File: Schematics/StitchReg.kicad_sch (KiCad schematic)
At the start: 10 parts, among them J1 Barrel_Jack, J2 DIN-6, K1 DIPxx-1Axx-11x, SW1 SW_Push, U1 MCP4131-xxxx-P

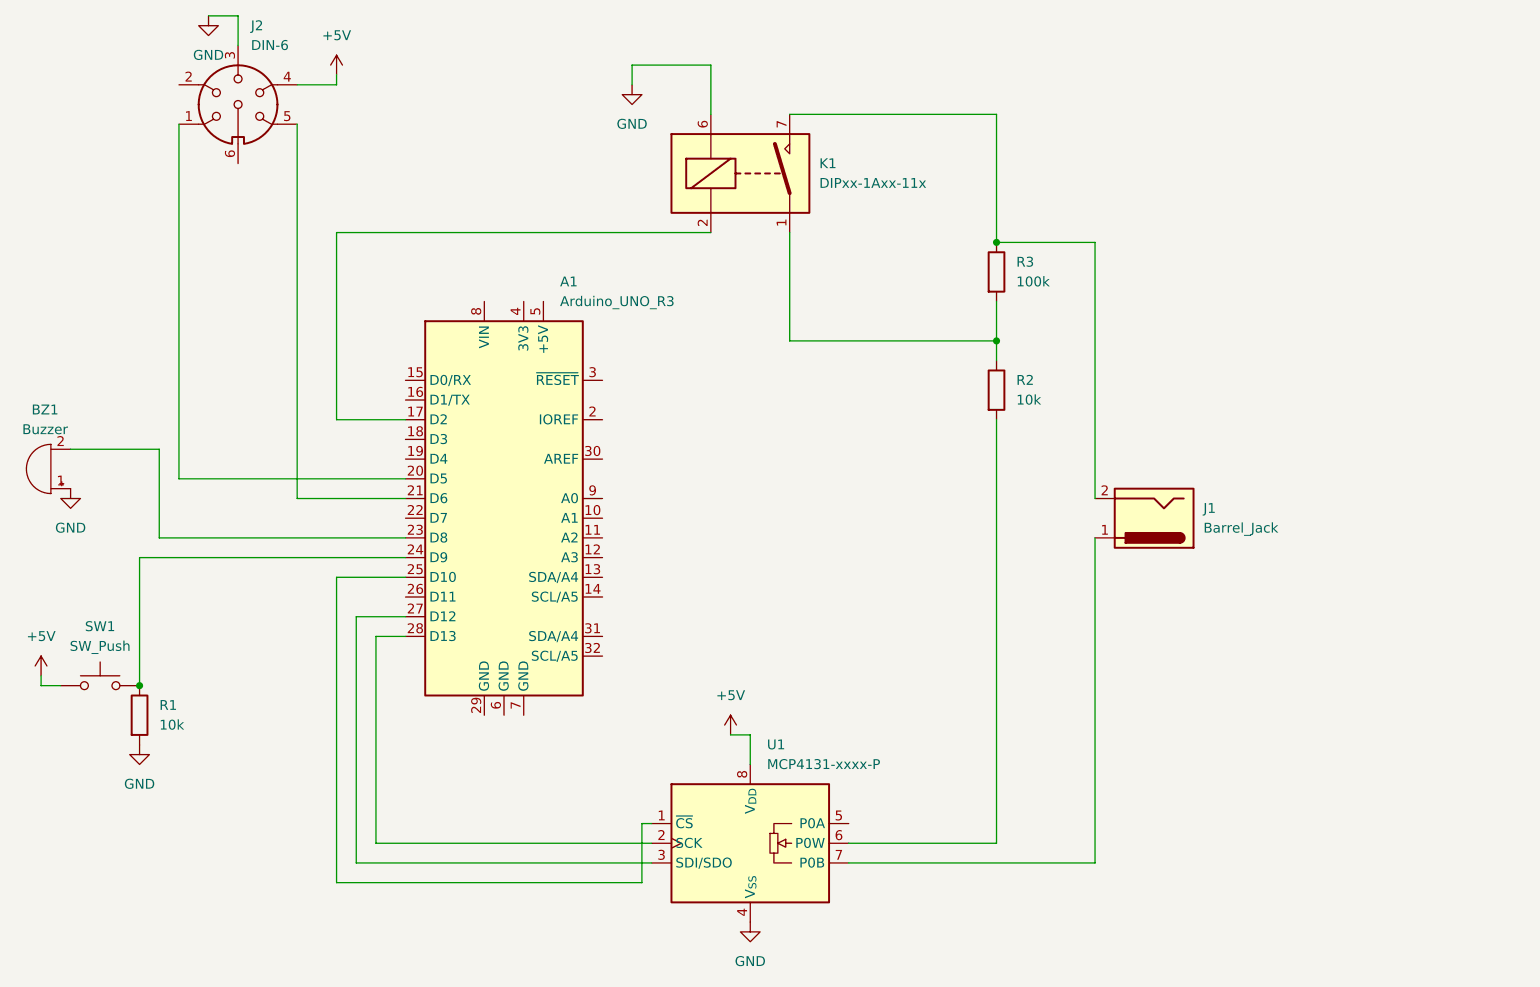
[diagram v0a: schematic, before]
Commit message: update schematic
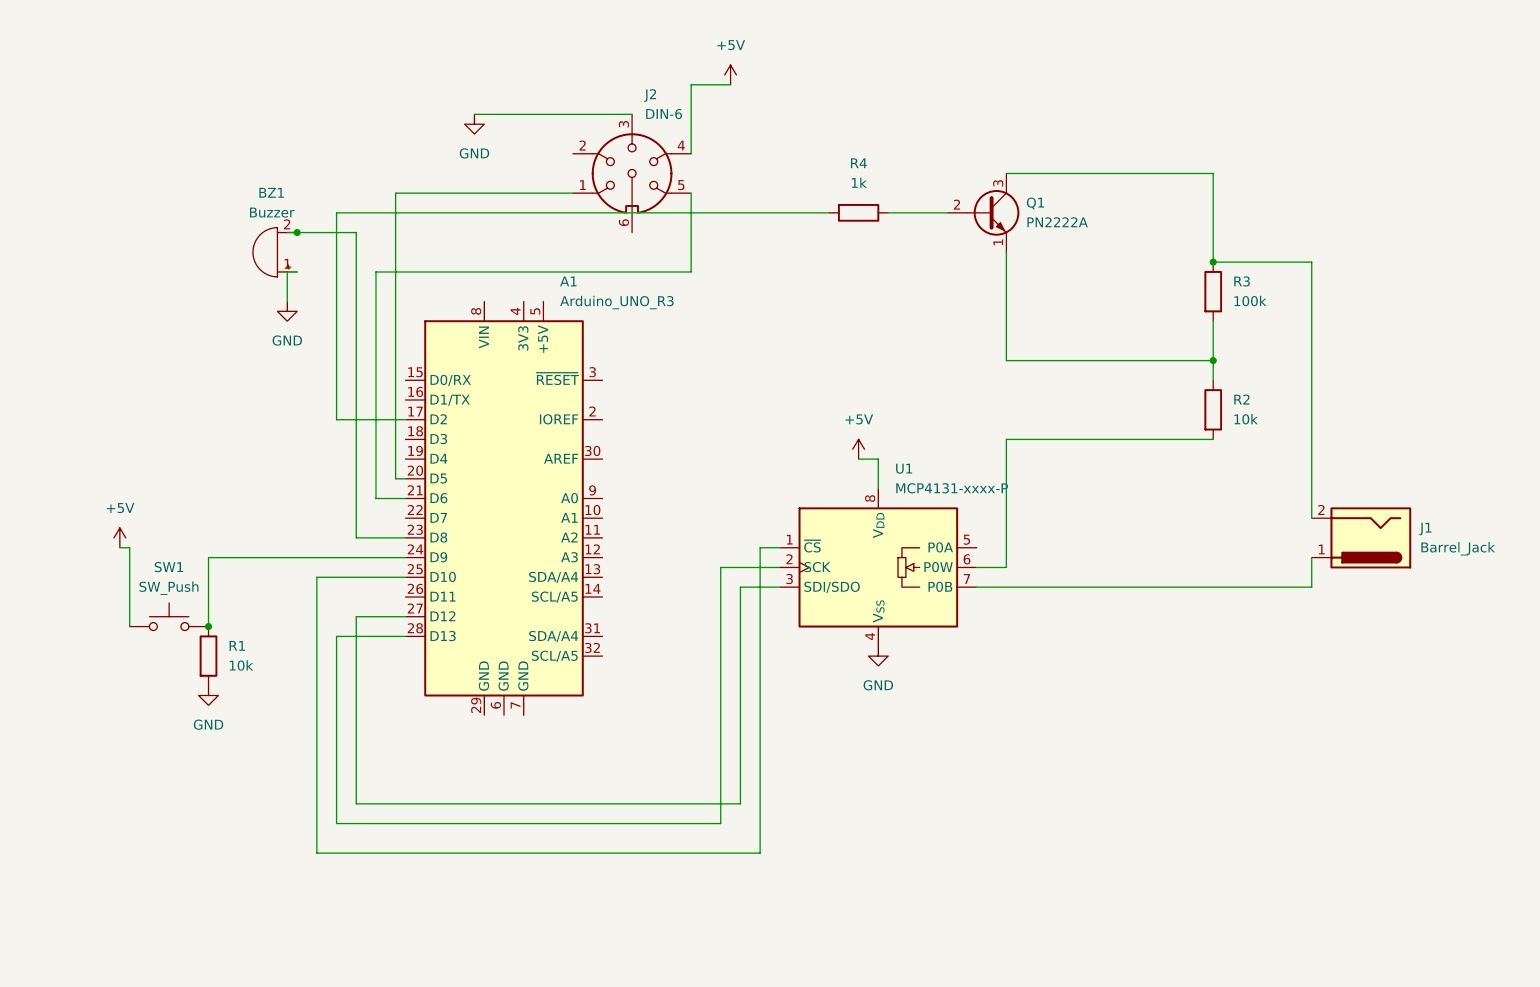
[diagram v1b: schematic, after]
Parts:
- removed K1: DIPxx-1Axx-11x, Relay_THT:Relay_StandexMeder_DIP_LowProfile, symbol Relay:DIPxx-1Axx-11x
- added Q1: PN2222A, Package_TO_SOT_THT:TO-92_Inline, symbol Transistor_BJT:PN2222A
- added R4: 1k, symbol Device:R
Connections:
- net at R2.1, R3.2: now also Q1.1 (E)
- net at A1.17 (D2): now also R4.2
- net at J1.2, R3.1: now also Q1.3 (C)
- new net: Q1.2 (B), R4.1
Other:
- moved on the sheet: BZ1, J1, J2, R1, R2, R3, SW1, U1
